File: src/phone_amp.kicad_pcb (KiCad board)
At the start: 2 copper layers, 11.6 x 56.1 mm, 41 parts, among them J1 M_USB_B, J2 PJ313D, J3 PJ313D, J4 RJ9_4P4C, J5 RJ9_4P4C, SW1 SWITCH_INV, U1 TPA6139A2, U2 MCP6024, U3 TC1017

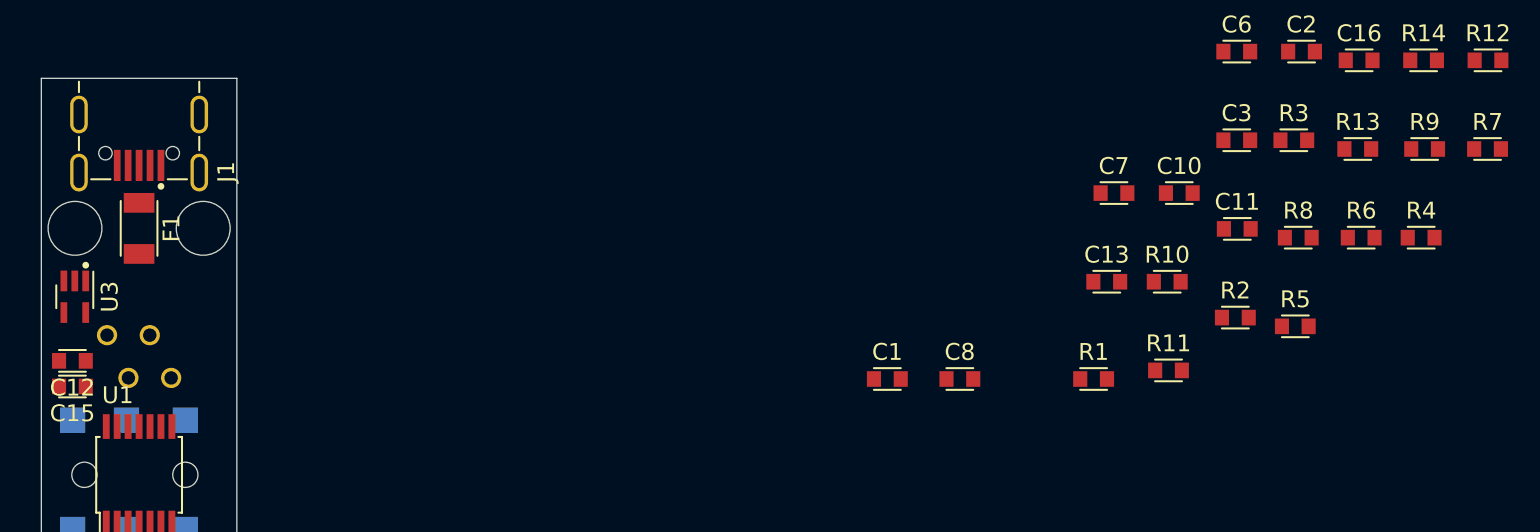
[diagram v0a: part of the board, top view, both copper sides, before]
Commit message: Placed fuse.
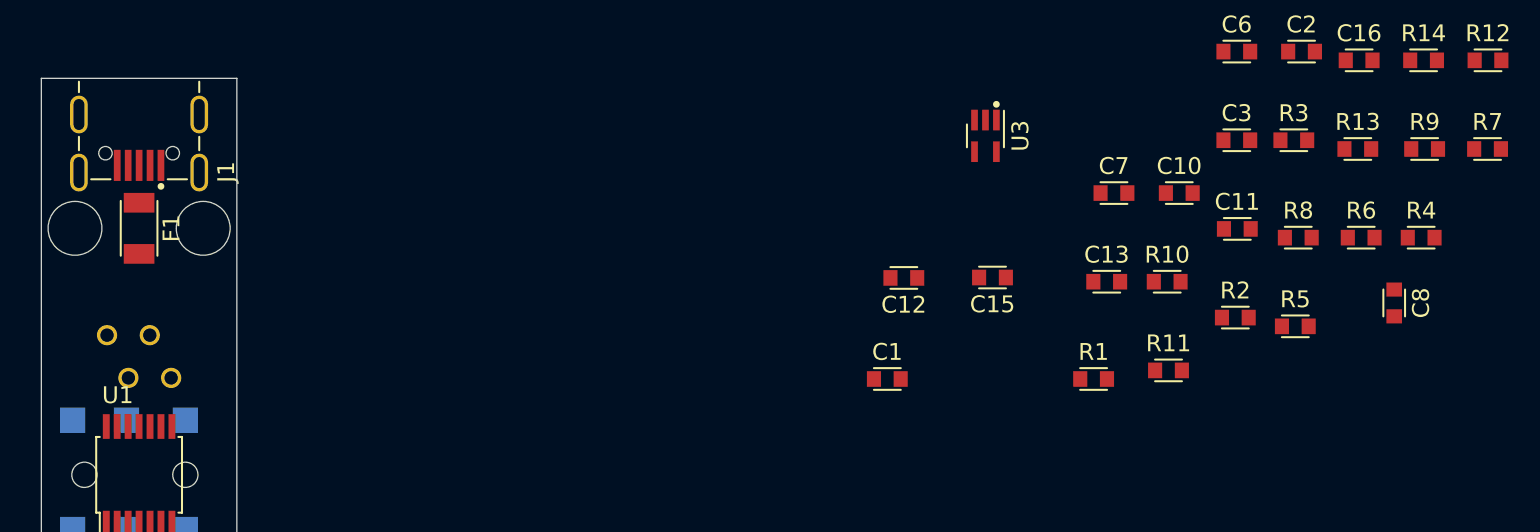
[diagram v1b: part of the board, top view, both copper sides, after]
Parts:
- moved C15 55.1 mm to (190.4, 91.2)
- moved U3 55.0 mm to (190.0, 82.8)
- moved C12 49.7 mm to (185.2, 91.2)
- moved C8 26.2 mm to (214.3, 92.7), turned to 270 degrees
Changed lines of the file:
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@@
     (36 B.SilkS user hide)
     (37 F.SilkS user hide)
-    (38 B.Mask user)
-    (39 F.Mask user)
+    (38 B.Mask user hide)
+    (39 F.Mask user hide)
     (40 Dwgs.User user)
     (41 Cmts.User user)
@@
     (44 Edge.Cuts user)
     (45 Margin user)
-    (46 B.CrtYd user)
-    (47 F.CrtYd user)
+    (46 B.CrtYd user hide)
+    (47 F.CrtYd user hide)
     (48 B.Fab user hide)
     (49 F.Fab user hide)
@@
     (aux_axis_origin 132.7404 136.8425)
     (grid_origin 132.7404 136.8425)
-    (visible_elements 7FFEF77F)
+    (visible_elements 7FFCF77F)
     (pcbplotparams
       (layerselection 0x00030_80000001)
@@
   )
   (module footprints:CHIP-0603 (layer F.Cu)
-    (at 188.482952 97.2546)
-    (fp_text reference C8 (at 0 -1.6002) (layer F.SilkS)
-      (effects (font (size 1 1) (thickness 0.15)))
-    )
-    (fp_text value 220n (at 0 1.5748) (layer F.Fab) hide
-      (effects (font (size 1 1) (thickness 0.15)))
-    )
-    (fp_line (start -1.47 -0.72) (end -1.47 0.72) (layer F.CrtYd) (width 0.05))
-    (fp_line (start -1.47 0.72) (end 1.47 0.72) (layer F.CrtYd) (width 0.05))
-    (fp_line (start 1.47 0.72) (end 1.47 -0.72) (layer F.CrtYd) (width 0.05))
-    (fp_line (start 1.47 -0.72) (end -1.47 -0.72) (layer F.CrtYd) (width 0.05))
-    (fp_line (start 0 -0.35) (end 0 0.35) (layer F.CrtYd) (width 0.05))
-    (fp_line (start 0.35 0) (end -0.35 0) (layer F.CrtYd) (width 0.05))
-    (fp_circle (center 0 0) (end -0.25 0) (layer F.CrtYd) (width 0.05))
-    (fp_line (start 0.85 -0.45) (end -0.85 -0.45) (layer F.Fab) (width 0.12))
-    (fp_line (start 0.85 0.45) (end 0.85 -0.45) (layer F.Fab) (width 0.12))
-    (fp_line (start -0.85 0.45) (end 0.85 0.45) (layer F.Fab) (width 0.12))
-    (fp_line (start -0.85 -0.45) (end -0.85 0.45) (layer F.Fab) (width 0.12))
-    (fp_line (start 0.8 0.645) (end -0.8 0.645) (layer F.SilkS) (width 0.12))
-    (fp_line (start 0.8 -0.645) (end -0.8 -0.645) (layer F.SilkS) (width 0.12))
-    (pad 1 smd rect (at -0.795 0) (size 0.84 0.93) (layers F.Cu F.Paste F.Mask)
+    (at 214.2998 92.7354 270)
+    (fp_text reference C8 (at 0 -1.6002 270) (layer F.SilkS)
+      (effects (font (size 1 1) (thickness 0.15)))
+    )
+    (fp_text value 220n (at 0 1.5748 270) (layer F.Fab) hide
+      (effects (font (size 1 1) (thickness 0.15)))
+    )
+    (fp_line (start -1.47 -0.72) (end -1.47 0.72) (layer F.CrtYd) (width 0.05))
+    (fp_line (start -1.47 0.72) (end 1.47 0.72) (layer F.CrtYd) (width 0.05))
+    (fp_line (start 1.47 0.72) (end 1.47 -0.72) (layer F.CrtYd) (width 0.05))
+    (fp_line (start 1.47 -0.72) (end -1.47 -0.72) (layer F.CrtYd) (width 0.05))
+    (fp_line (start 0 -0.35) (end 0 0.35) (layer F.CrtYd) (width 0.05))
+    (fp_line (start 0.35 0) (end -0.35 0) (layer F.CrtYd) (width 0.05))
+    (fp_circle (center 0 0) (end -0.25 0) (layer F.CrtYd) (width 0.05))
+    (fp_line (start 0.85 -0.45) (end -0.85 -0.45) (layer F.Fab) (width 0.12))
+    (fp_line (start 0.85 0.45) (end 0.85 -0.45) (layer F.Fab) (width 0.12))
+    (fp_line (start -0.85 0.45) (end 0.85 0.45) (layer F.Fab) (width 0.12))
+    (fp_line (start -0.85 -0.45) (end -0.85 0.45) (layer F.Fab) (width 0.12))
+    (fp_line (start 0.8 0.645) (end -0.8 0.645) (layer F.SilkS) (width 0.12))
+    (fp_line (start 0.8 -0.645) (end -0.8 -0.645) (layer F.SilkS) (width 0.12))
+    (pad 1 smd rect (at -0.795 0 270) (size 0.84 0.93) (layers F.Cu F.Paste F.Mask)
       (net 14 HP_MIC_OUT))
-    (pad 2 smd rect (at 0.795 0) (size 0.84 0.93) (layers F.Cu F.Paste F.Mask)
+    (pad 2 smd rect (at 0.795 0 270) (size 0.84 0.93) (layers F.Cu F.Paste F.Mask)
       (net 8 "Net-(C5-Pad1)"))
   )
@@
   )
   (module footprints:CHIP-0603 (layer F.Cu)
-    (at 135.7376 96.1771 180)
+    (at 185.1533 91.2495 180)
     (fp_text reference C12 (at 0 -1.6002 180) (layer F.SilkS)
       (effects (font (size 1 1) (thickness 0.15)))
@@
   )
   (module footprints:CHIP-0603 (layer F.Cu)
-    (at 135.7376 97.7011 180)
+    (at 190.4238 91.2241 180)
     (fp_text reference C15 (at 0 -1.6002 180) (layer F.SilkS)
       (effects (font (size 1 1) (thickness 0.15)))
@@
   )
   (module footprints:FUSE-1206 (layer F.Cu)
-    (at 139.7 88.3031 270)
+    (at 139.7 88.3 270)
     (fp_text reference F1 (at 0 -1.9304 270) (layer F.SilkS)
       (effects (font (size 1 1) (thickness 0.15)))
@@
   )
   (module footprints:SC-70 (layer F.Cu)
-    (at 135.8773 92.3671 180)
+    (at 190.0047 82.804 180)
     (fp_text reference U3 (at -2.0828 0 270) (layer F.SilkS)
       (effects (font (size 1 1) (thickness 0.15)))

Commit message: Updated schematic and related files.
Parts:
- moved C14 95.4 mm to (135.4, 106.4), turned to 180 degrees
- moved R12 93.3 mm to (135.4, 118.0), turned to 180 degrees
- moved C4 86.4 mm to (144.0, 116.4)
- moved R14 85.9 mm to (135.4, 108.0), turned to 180 degrees
- moved C5 85.6 mm to (135.4, 98.0), turned to 180 degrees
- moved C9 82.7 mm to (144.0, 114.9)
- moved R15 81.3 mm to (144.0, 94.9)
- moved C16 80.1 mm to (135.4, 101.0), turned to 180 degrees
- moved R13 79.6 mm to (135.4, 104.9), turned to 180 degrees
- moved R7 77.9 mm to (144.0, 101.0)
- moved R9 77.2 mm to (144.0, 111.0), turned to 180 degrees
- moved C2 76.3 mm to (144.0, 118.0)
- moved C8 75.2 mm to (144.0, 119.5), turned to 180 degrees
- moved C3 74.9 mm to (135.4, 111.0), turned to 180 degrees
- moved C11 74.4 mm to (135.4, 114.9)
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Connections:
- J1 pad 2: Net-(J1-Pad2) -> (no net)
- J1 pad 3: Net-(J1-Pad3) -> (no net)
- J1 pad 4: Net-(J1-Pad4) -> (no net)
- J2 pad 1: HP_MIC -> (no net)
- J2 pad 2: HP_MIC_BIAS -> (no net)
- J3 pad 1: HP_SPK_L -> (no net)
- J3 pad 5: HP_SPK_R -> (no net)
- R3 pad 1: HS_SPK_N -> HS_SPK_P
- R4 pad 1: HS_SPK_P -> HS_SPK_N
- U1 pad 7: Net-(U1-Pad7) -> (no net)
- U1 pad 8: Net-(U1-Pad8) -> (no net)
- U2 pad 1: Net-(C5-Pad1) -> VGND
- U2 pad 12: Net-(C14-Pad1) -> VGND
- U2 pad 13: VGND -> Net-(C5-Pad2)
- U2 pad 14: VGND -> Net-(C5-Pad1)
- U2 pad 2: Net-(C5-Pad2) -> VGND
- U2 pad 3: VGND -> Net-(C14-Pad1)
- U3 pad 2: Net-(U3-Pad2) -> (no net)
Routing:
- net GND: track 0.00 -> 103.9 mm, vias 0 -> 4
- net HS_SPK_P: track 0.00 -> 51.5 mm
- net HS_SPK_N: track 0.00 -> 49.7 mm
- net PHONE_MIC_P: track 0.00 -> 47.6 mm, vias 0 -> 1
- net +3V3: track 0.00 -> 33.4 mm, vias 0 -> 1
- net Net-(C5-Pad1): track 0.00 -> 33.0 mm, vias 0 -> 2
- net VGND: track 0.00 -> 32.7 mm, vias 0 -> 3
- net Net-(R11-Pad2): track 0.00 -> 25.5 mm, vias 0 -> 2
- net Net-(C9-Pad1): track 0.00 -> 21.5 mm
- net HP_SPK_PRE: track 0.00 -> 15.1 mm
- net HP_MUTE: track 0.00 -> 14.8 mm, vias 0 -> 2
- net HP_MIC_OUT: track 0.00 -> 14.5 mm
- net HP_MIC_BIAS: track 0.00 -> 14.0 mm, vias 0 -> 1
- net HS_MIC_P: track 0.00 -> 13.2 mm
- net HP_MIC: track 0.00 -> 11.1 mm, vias 0 -> 1
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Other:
- rule via_min_drill: 0.3 -> 0.4
- rule via_min_size: 0.4 -> 0.2

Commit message: Made modifications to pcb.
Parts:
- moved R11 8.68 mm to (144.0, 121.0)
- moved R8 8.68 mm to (135.4, 119.5), turned to 180 degrees
- moved C8 8.68 mm to (135.4, 118.0), turned to 0 degrees
- moved R12 8.68 mm to (144.0, 119.5)
- moved C12 8.54 mm to (144.0, 93.3)
- moved C15 8.54 mm to (135.4, 93.3), turned to 180 degrees
- turned U3 to 90 degrees
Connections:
- J1 pad 2: (no net) -> Net-(J1-Pad2)
- J1 pad 3: (no net) -> Net-(J1-Pad3)
- J1 pad 4: (no net) -> Net-(J1-Pad4)
- J2 pad 1: (no net) -> Net-(J2-Pad1)
- J2 pad 2: (no net) -> Net-(J2-Pad2)
- J3 pad 1: (no net) -> Net-(J3-Pad1)
- J3 pad 5: (no net) -> Net-(J3-Pad5)
- J5 pad 2: HS_SPK_N -> HS_SPK_P
- J5 pad 3: HS_SPK_P -> HS_SPK_N
- SW1 pad 1: HS_MIC_P -> HP_MIC_OUT
- SW1 pad 3: HP_MIC_OUT -> HS_MIC_P
- U1 pad 7: (no net) -> Net-(U1-Pad7)
- U1 pad 8: (no net) -> Net-(U1-Pad8)
- U3 pad 2: (no net) -> Net-(U3-Pad2)
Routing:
- net +3V3: track 33.4 -> 63.9 mm, vias 1 -> 3
- net HS_SPK_P: track 51.5 -> 28.5 mm
- net Net-(R11-Pad2): track 25.5 -> 9.45 mm, vias 2 -> 1
- net HP_MUTE: track 14.8 -> 0.00 mm, vias 2 -> 0
- net HS_SPK_N: track 49.7 -> 41.7 mm
- net VGND: track 32.7 -> 25.0 mm, vias 3 -> 2
- net GND: track 103.9 -> 109.7 mm
- net Net-(C12-Pad2): track 9.33 -> 6.38 mm
- net HP_MIC_BIAS: track 14.0 -> 11.3 mm
- net HS_MIC_P: track 13.2 -> 10.5 mm
- net Net-(C5-Pad1): track 33.0 -> 31.0 mm
- net Net-(C14-Pad1): track 10.1 -> 8.45 mm
- net HP_SPK_R: track 4.73 -> 6.23 mm
- net HP_MIC_OUT: track 14.5 -> 15.1 mm

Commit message: Made some pcb changes.
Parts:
- moved R15 8.68 mm to (135.4, 93.3), turned to 180 degrees
- moved C16 6.92 mm to (135.4, 108.0), turned to 0 degrees
- moved R13 3.84 mm to (135.4, 101.0), turned to 0 degrees
- moved C12 1.57 mm to (144.0, 94.9)
- moved C15 1.57 mm to (135.4, 91.7)
- moved R14 1.54 mm to (135.4, 106.4)
- moved C14 1.54 mm to (135.4, 104.9)
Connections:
- J1 pad 2: Net-(J1-Pad2) -> (no net)
- J1 pad 3: Net-(J1-Pad3) -> (no net)
- J1 pad 4: Net-(J1-Pad4) -> (no net)
- J2 pad 1: Net-(J2-Pad1) -> (no net)
- J2 pad 2: Net-(J2-Pad2) -> (no net)
- J3 pad 1: Net-(J3-Pad1) -> HP_SPK_R
- J3 pad 2: HP_SPK_R -> (no net)
- J3 pad 5: Net-(J3-Pad5) -> HP_SPK_L
- J3 pad 6: HP_SPK_L -> (no net)
- U1 pad 7: Net-(U1-Pad7) -> (no net)
- U1 pad 8: Net-(U1-Pad8) -> (no net)
- U3 pad 2: Net-(U3-Pad2) -> (no net)
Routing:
- net Net-(R11-Pad2): track 9.45 -> 29.7 mm, vias 1 -> 2
- net HP_MUTE: track 0.00 -> 13.8 mm, vias 0 -> 2
- net GND: track 109.7 -> 123.1 mm, vias 4 -> 6
- net VGND: track 25.0 -> 34.8 mm
- net HS_SPK_N: track 41.7 -> 47.1 mm
- net Net-(C12-Pad2): track 6.38 -> 8.94 mm
- net HP_SPK_L: track 4.07 -> 6.43 mm
- net Net-(C14-Pad1): track 8.45 -> 10.5 mm
- net HP_MIC: track 11.4 -> 10.0 mm
- net HP_MIC_BIAS: track 11.3 -> 9.94 mm
- net HS_SPK_P: track 28.5 -> 29.8 mm
- net Net-(C5-Pad2): track 10.6 -> 9.41 mm
- net Net-(C9-Pad1): track 21.5 -> 22.1 mm
- net +3V3: track 63.9 -> 63.5 mm, vias 3 -> 4

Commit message: Updated PCB.
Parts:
- turned U3 to 270 degrees
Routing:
- net GND: track 123.1 -> 132.1 mm, vias 6 -> 8
- net +3V3: track 63.5 -> 70.9 mm, vias 4 -> 6
- net HS_SPK_N: track 47.1 -> 43.6 mm
- net Net-(C12-Pad2): track 8.94 -> 12.2 mm
- net HS_SPK_P: track 29.8 -> 32.0 mm
- net HP_MIC_OUT: track 15.1 -> 16.2 mm
- net HP_MIC: track 10.0 -> 11.1 mm
- net Net-(C13-Pad2): track 8.98 -> 8.01 mm
- net PHONE_MIC_P: track 47.7 -> 48.7 mm
- net HP_SPK_PRE: track 14.9 -> 14.2 mm
- net HP_MIC_BIAS: track 9.94 -> 9.24 mm
- net Net-(C5-Pad2): track 9.41 -> 8.83 mm

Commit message: Uploaded finished design.
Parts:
- added G***: LOGO, footprints:OSH_LOGO, F.Cu at (139.7, 124.5)
- C1, C10, C11, C12, C13, C14, C15, C16, C2, C3, C4, C5, C6, C7, C8, C9, R1, R10, R11, R12, R13, R14, R15, R2, R3, R4, R5, R6, R7, R8, R9: footprint footprints:CHIP-0603 -> footprints:CHIP-0603-NO-SILK
- F1: footprint footprints:FUSE-1206 -> footprints:FUSE-1206-NO-SILK
- J1: footprint footprints:USB-MICRO-TH -> footprints:USB-MICRO-TH-NO-SILK
- J2, J3: footprint footprints:JACK-3.5MM -> footprints:JACK-3.5MM-NO-SILK
- J4, J5: footprint footprints:RJ9-4P4C -> footprints:RJ9-4P4C-NO-SILK
- SW1: footprint footprints:SWITCH-SPDT -> footprints:SWITCH-SPDT-NO-SILK
- U1, U2: footprint footprints:TSSOP-14 -> footprints:TSSOP-14-NO-SILK
- U3: footprint footprints:SC-70 -> footprints:SC-70-NO-SILK
- moved C15 9.10 mm to (144.0, 94.9)
- moved C12 1.57 mm to (144.0, 93.3)
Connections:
- J1 pad 2: (no net) -> Net-(J1-Pad2)
- J1 pad 3: (no net) -> Net-(J1-Pad3)
- J1 pad 4: (no net) -> Net-(J1-Pad4)
- J2 pad 1: (no net) -> Net-(J2-Pad1)
- J2 pad 2: (no net) -> Net-(J2-Pad2)
- J3 pad 2: (no net) -> Net-(J3-Pad2)
- J3 pad 6: (no net) -> Net-(J3-Pad6)
- U1 pad 7: (no net) -> Net-(U1-Pad7)
- U1 pad 8: (no net) -> Net-(U1-Pad8)
- U3 pad 2: (no net) -> Net-(U3-Pad2)
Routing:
- net GND: track 132.1 -> 155.1 mm, vias 8 -> 13
- net HS_SPK_P: track 32.0 -> 29.2 mm
- net Net-(C12-Pad2): track 12.2 -> 9.50 mm
- net +3V3: track 70.9 -> 73.3 mm
- net Net-(R11-Pad2): track 29.4 -> 30.8 mm
- net HP_MUTE: track 13.8 -> 14.7 mm
- net PHONE_MIC_P: track 48.7 -> 47.9 mm
- added copper zone on B.Cu, net GND
- added copper zone on F.Cu, net GND
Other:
- board text added: "github iocapa"

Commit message: Sent to production.
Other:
- board text added: "V.1"

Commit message: Tested. Ready for small batches
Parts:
- R15: value 3.3k -> 2.2k
- R8: value 3.3k -> 4.3k
